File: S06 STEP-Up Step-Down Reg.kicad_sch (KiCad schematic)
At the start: 57 parts, among them Q16 IAUCN04S7L019, Q17 IAUCN04S7L028, Q18 CSD17304Q3, Q19 IAUCN04S7L019, U5 LM51772RHAR

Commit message: Gate resistors placed, snubbers at the low-side FETs in EVM order, H1/H2/LOGO01 symbols
- R111-R114 (3R 0603) placed and routed next to the Q16-Q19 gates, each fed
  from In6 through a via in its driver-side pad.
- Snubbers reordered to match TI's LM51772EVM-HP (switch node -> C -> R -> GND)
  and moved to the low-side FETs: C39 on Q19's drain edge with R45 to GND,
  C35 on Q17's drain leads with R41 to GND, two In1 vias at each R GND pad.
  The top-copper SW1/SW2 pour lobes for the old positions are removed.
- H1, H2 (Mechanical:MountingHole_Pad, pin 1 to GND) and LOGO01 (pinless
  EVOSONIC_LOGO symbol) added to the root sheet and linked to their existing
  footprints, so Update PCB from Schematic no longer deletes them. The
  mounting-hole footprint is saved as MountingHole_3.2mm_Pad_7.4mm.
- ERC 0; DRC 0 unconnected, 0 parity, no courtyard overlaps.

Co-Authored-By: Claude Opus 5.5 <noreply@anthropic.com>
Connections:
- net GND: now also R41.1, R45.1; no longer C35.1, C39.1
- net SW1: now also C35.2; no longer R41.2
- net SW2: now also C39.2; no longer R45.2
- new net: C39.1, R45.2
- new net: C35.1, R41.2
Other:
- moved on the sheet: C35, C39, R41, R45
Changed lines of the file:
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@@
 	(symbol
 		(lib_id "Device:C")
-		(at 227.33 88.9 180)
+		(at 227.33 78.74 180)
 		(unit 1)
 		(body_style 1)
@@
 		(dnp no)
 		(property "Reference" "C39"
-			(at 228.6 88.646 0)
+			(at 228.6 78.486 0)
 			(show_name no)
 			(do_not_autoplace no)
@@
 		)
 		(property "Value" "1nF"
-			(at 228.6 91.186 0)
+			(at 228.6 81.026 0)
 			(show_name no)
 			(do_not_autoplace no)
@@
 		)
 		(property "Footprint" "Capacitor_SMD:C_0805_2012Metric"
-			(at 227.33 88.9 90)
+			(at 227.33 78.74 90)
 			(hide yes)
 			(show_name no)
@@
 		)
 		(property "Datasheet" ""
-			(at 227.33 88.9 90)
+			(at 227.33 78.74 90)
 			(hide yes)
 			(show_name no)
@@
 		)
 		(property "Description" "Capacitor 1nF 50V X7R 0805"
-			(at 227.33 88.9 90)
+			(at 227.33 78.74 90)
 			(hide yes)
 			(show_name no)
@@
 		)
 		(property "NOTE" ""
-			(at 226.822 86.36 0)
+			(at 226.822 76.2 0)
 			(hide yes)
 			(show_name no)
@@
 		)
 		(property "PL_SORT_GROUP" ""
-			(at 226.822 86.36 0)
+			(at 226.822 76.2 0)
 			(hide yes)
 			(show_name no)
@@
 		)
 		(property "MANUFACTURER" ""
-			(at 223.012 85.09 0)
+			(at 223.012 74.93 0)
 			(hide yes)
 			(show_name no)
@@
 		)
 		(property "MANUFACTURER_PN" ""
-			(at 223.012 85.09 0)
+			(at 223.012 74.93 0)
 			(hide yes)
 			(show_name no)
@@
 		)
 		(property "ALTIUM_VALUE" "1nF"
-			(at 224.79 91.44 0)
+			(at 224.79 81.28 0)
 			(hide yes)
 			(show_name no)
@@
 		)
 		(property "ALTIUM_FOOTPRINT" "0805"
-			(at 228.6 93.218 0)
+			(at 228.6 83.058 0)
 			(show_name no)
 			(do_not_autoplace no)
@@
 		)
 		(property "MATERIAL" "X7R"
-			(at 228.6 95.25 0)
+			(at 228.6 85.09 0)
 			(show_name no)
 			(do_not_autoplace no)
@@
 		)
 		(property "VOLTAGE" "50V"
-			(at 228.6 97.79 0)
+			(at 228.6 87.63 0)
 			(show_name no)
 			(do_not_autoplace no)
@@
 	(symbol
 		(lib_id "Device:R")
-		(at 182.88 78.74 180)
+		(at 182.88 88.9 180)
 		(unit 1)
 		(body_style 1)
@@
 		(dnp no)
 		(property "Reference" "R41"
-			(at 183.896 78.74 0)
+			(at 183.896 88.9 0)
 			(show_name no)
 			(do_not_autoplace no)
@@
 		)
 		(property "Value" "2.2R"
-			(at 183.896 81.28 0)
+			(at 183.896 91.44 0)
 			(show_name no)
 			(do_not_autoplace no)
@@
 		)
 		(property "Footprint" "Resistor_SMD:R_1210_3225Metric"
-			(at 182.88 78.74 90)
+			(at 182.88 88.9 90)
 			(hide yes)
 			(show_name no)
@@
 		)
 		(property "Datasheet" ""
-			(at 182.88 78.74 90)
+			(at 182.88 88.9 90)
 			(hide yes)
 			(show_name no)
@@
 		)
 		(property "Description" "Resistor 2.2R 1% 1/2W 1210"
-			(at 182.88 78.74 90)
+			(at 182.88 88.9 90)
 			(hide yes)
 			(show_name no)
@@
 		)
 		(property "NOTE" ""
-			(at 181.864 74.422 0)
+			(at 181.864 84.582 0)
 			(hide yes)
 			(show_name no)
@@
 		)
 		(property "PL_SORT_GROUP" ""
-			(at 181.864 74.422 0)
+			(at 181.864 84.582 0)
 			(hide yes)
 			(show_name no)
@@
 		)
 		(property "MANUFACTURER" ""
-			(at 181.864 74.422 0)
+			(at 181.864 84.582 0)
 			(hide yes)
 			(show_name no)
@@
 		)
 		(property "MANUFACTURER_PN" ""
-			(at 181.864 74.422 0)
+			(at 181.864 84.582 0)
 			(hide yes)
 			(show_name no)
@@
 		)
 		(property "ALTIUM_VALUE" "2.2R"
-			(at 181.864 74.422 0)
+			(at 181.864 84.582 0)
 			(hide yes)
 			(show_name no)
@@
 		)
 		(property "ALTIUM_FOOTPRINT" "1210"
-			(at 183.896 83.312 0)
+			(at 183.896 93.472 0)
 			(show_name no)
 			(do_not_autoplace no)
@@
 	(symbol
 		(lib_id "Device:C")
-		(at 182.88 88.9 180)
+		(at 182.88 78.74 180)
 		(unit 1)
 		(body_style 1)
@@
 		(dnp no)
 		(property "Reference" "C35"
-			(at 184.15 88.646 0)
+			(at 184.15 78.486 0)
 			(show_name no)
 			(do_not_autoplace no)
@@
 		)
 		(property "Value" "470pF"
-			(at 184.15 91.186 0)
+			(at 184.15 81.026 0)
 			(show_name no)
 			(do_not_autoplace no)
@@
 		)
 		(property "Footprint" "Capacitor_SMD:C_0805_2012Metric"
-			(at 182.88 88.9 90)
+			(at 182.88 78.74 90)
 			(hide yes)
 			(show_name no)
@@
 		)
 		(property "Datasheet" ""
-			(at 182.88 88.9 90)
+			(at 182.88 78.74 90)
 			(hide yes)
 			(show_name no)
@@
 		)
 		(property "Description" "Capacitor 470pF 50V X7R 0805"
-			(at 182.88 88.9 90)
+			(at 182.88 78.74 90)
 			(hide yes)
 			(show_name no)
@@
 		)
 		(property "NOTE" ""
-			(at 182.372 86.36 0)
+			(at 182.372 76.2 0)
 			(hide yes)
 			(show_name no)
@@
 		)
 		(property "PL_SORT_GROUP" ""
-			(at 182.372 86.36 0)
+			(at 182.372 76.2 0)
 			(hide yes)
 			(show_name no)
@@
 		)
 		(property "MANUFACTURER" ""
-			(at 178.562 85.09 0)
+			(at 178.562 74.93 0)
 			(hide yes)
 			(show_name no)
@@
 		)
 		(property "MANUFACTURER_PN" ""
-			(at 178.562 85.09 0)
+			(at 178.562 74.93 0)
 			(hide yes)
 			(show_name no)
@@
 		)
 		(property "ALTIUM_VALUE" "470pF"
-			(at 180.34 91.44 0)
+			(at 180.34 81.28 0)
 			(hide yes)
 			(show_name no)
@@
 		)
 		(property "ALTIUM_FOOTPRINT" "0805"
-			(at 184.15 93.218 0)
+			(at 184.15 83.058 0)
 			(show_name no)
 			(do_not_autoplace no)
@@
 		)
 		(property "MATERIAL" "X7R"
-			(at 184.15 95.25 0)
+			(at 184.15 85.09 0)
 			(show_name no)
 			(do_not_autoplace no)
@@
 		)
 		(property "VOLTAGE" "50V"
-			(at 184.15 97.79 0)
+			(at 184.15 87.63 0)
 			(show_name no)
 			(do_not_autoplace no)
@@
 	(symbol
 		(lib_id "Device:R")
-		(at 227.33 78.74 180)
+		(at 227.33 88.9 180)
 		(unit 1)
 		(body_style 1)
@@
 		(dnp no)
 		(property "Reference" "R45"
-			(at 228.346 78.74 0)
+			(at 228.346 88.9 0)
 			(show_name no)
 			(do_not_autoplace no)
@@
 		)
 		(property "Value" "2.2R"
-			(at 228.346 81.28 0)
+			(at 228.346 91.44 0)
 			(show_name no)
 			(do_not_autoplace no)
@@
 		)
 		(property "Footprint" "Resistor_SMD:R_1210_3225Metric"
-			(at 227.33 78.74 90)
+			(at 227.33 88.9 90)
 			(hide yes)
 			(show_name no)
@@
 		)
 		(property "Datasheet" ""
-			(at 227.33 78.74 90)
+			(at 227.33 88.9 90)
 			(hide yes)
 			(show_name no)
@@
 		)
 		(property "Description" "Resistor 2.2R 1% 1/2W 1210"
-			(at 227.33 78.74 90)
+			(at 227.33 88.9 90)
 			(hide yes)
 			(show_name no)
@@
 		)
 		(property "NOTE" ""
-			(at 226.314 74.422 0)
+			(at 226.314 84.582 0)
 			(hide yes)
 			(show_name no)
@@
 		)
 		(property "PL_SORT_GROUP" ""
-			(at 226.314 74.422 0)
+			(at 226.314 84.582 0)
 			(hide yes)
 			(show_name no)
@@
 		)
 		(property "MANUFACTURER" ""
-			(at 226.314 74.422 0)
+			(at 226.314 84.582 0)
 			(hide yes)
 			(show_name no)
@@
 		)
 		(property "MANUFACTURER_PN" ""
-			(at 226.314 74.422 0)
+			(at 226.314 84.582 0)
 			(hide yes)
 			(show_name no)
@@
 		)
 		(property "ALTIUM_VALUE" "2.2R"
-			(at 226.314 74.422 0)
+			(at 226.314 84.582 0)
 			(hide yes)
 			(show_name no)
@@
 		)
 		(property "ALTIUM_FOOTPRINT" "1210"
-			(at 228.346 83.312 0)
+			(at 228.346 93.472 0)
 			(show_name no)
 			(do_not_autoplace no)

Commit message: C60: 100 nF 0603 output HF cap at Q18's drain
Closes the boost hot loop at the FETs, as C7 on TI's LM51772EVM-HP.
Output pad has a via to the inner output planes; GND pad has two vias
to In1.

Co-Authored-By: Claude Opus 5.5 <noreply@anthropic.com>
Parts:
- added C60: 100nF, Capacitor_SMD:C_0603_1608Metric, symbol Device:C
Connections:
- net GND: now also C60.1
- net at C40.1, C41.1, C42.1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: now also C60.2
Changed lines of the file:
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@@
 		)
+	)
+	(symbol
+		(lib_id "Device:C")
+		(at 270.510 76.200 180)
+		(unit 1)
+		(body_style 1)
+		(exclude_from_sim no)
+		(in_bom yes)
+		(on_board yes)
+		(in_pos_files yes)
+		(dnp no)
+		(property "Reference" "C60"
+			(at 271.780 75.946 0)
+			(show_name no)
+			(do_not_autoplace no)
+			(effects
+				(font
+					(size 1.27 1.27)
+				)
+				(justify right bottom)
+			)
+		)
+		(property "Value" "100nF"
+			(at 271.780 78.486 0)
+			(show_name no)
+			(do_not_autoplace no)
+			(effects
+				(font
+					(size 1.27 1.27)
+				)
+				(justify right bottom)
+			)
+		)
+		(property "Footprint" "Capacitor_SMD:C_0603_1608Metric"
+			(at 270.510 76.200 90)
+			(hide yes)
+			(show_name no)
+			(do_not_autoplace no)
+			(effects
+				(font
+					(size 1.27 1.27)
+				)
+			)
+		)
+		(property "Datasheet" ""
+			(at 270.510 76.200 90)
+			(hide yes)
+			(show_name no)
+			(do_not_autoplace no)
+			(effects
+				(font
+					(size 1.27 1.27)
+				)
+			)
+		)
+		(property "Description" "Capacitor 100nF 50V X7R 0603"
+			(at 270.510 76.200 90)
+			(hide yes)
+			(show_name no)
+			(do_not_autoplace no)
+			(effects
+				(font
+					(size 1.27 1.27)
+				)
+			)
+		)
+		(property "NOTE" ""
+			(at 269.240 71.882 0)
+			(hide yes)
+			(show_name no)
+			(do_not_autoplace no)
+			(effects
+				(font
+					(size 1.27 1.27)
+				)
+				(justify right bottom)
+			)
+		)
+		(property "PL_SORT_GROUP" ""
+			(at 269.240 71.882 0)
+			(hide yes)
+			(show_name no)
+			(do_not_autoplace no)
+			(effects
+				(font
+					(size 1.27 1.27)
+				)
+				(justify right bottom)
+			)
+		)
+		(property "MANUFACTURER" ""
+			(at 269.240 71.882 0)
+			(hide yes)
+			(show_name no)
+			(do_not_autoplace no)
+			(effects
+				(font
+					(size 1.27 1.27)
+				)
+				(justify right bottom)
+			)
+		)
+		(property "MANUFACTURER_PN" ""
+			(at 269.240 71.882 0)
+			(hide yes)
+			(show_name no)
+			(do_not_autoplace no)
+			(effects
+				(font
+					(size 1.27 1.27)
+				)
+				(justify right bottom)
+			)
+		)
+		(property "ALTIUM_VALUE" "100nF"
+			(at 269.240 71.882 0)
+			(hide yes)
+			(show_name no)
+			(do_not_autoplace no)
+			(effects
+				(font
+					(size 1.27 1.27)
+				)
+				(justify right bottom)
+			)
+		)
+		(property "ALTIUM_FOOTPRINT" "0603"
+			(at 271.780 80.518 0)
+			(show_name no)
+			(do_not_autoplace no)
+			(effects
+				(font
+					(size 1.27 1.27)
+				)
+				(justify right bottom)
+			)
+		)
+		(property "MATERIAL" "X7R"
+			(at 271.780 82.550 0)
+			(show_name no)
+			(do_not_autoplace no)
+			(effects
+				(font
+					(size 1.27 1.27)
+				)
+				(justify right bottom)
+			)
+		)
+		(property "VOLTAGE" "50V"
+			(at 271.780 85.090 0)
+			(show_name no)
+			(do_not_autoplace no)
+			(effects
+				(font
+					(size 1.27 1.27)
+				)
+				(justify right bottom)
+			)
+		)
+		(pin "2"
+		)
+		(pin "1"
+		)
+		(instances
+			(project "EVO2513"
+				(path "/44203427-0a3b-455b-9bb9-c1b577d179b3/7e883a06-f690-476b-966b-7e93c32ca0bb"
+					(reference "C60")
+					(unit 1)
+				)
+			)
+		)
+	)
+	(wire
+		(pts
+			(xy 270.51 59.69) (xy 270.51 72.39)
+		)
+		(stroke
+			(width 0)
+			(type default)
+		)
+	)
+	(wire
+		(pts
+			(xy 270.51 80.01) (xy 270.51 92.71)
+		)
+		(stroke
+			(width 0)
+			(type default)
+		)
+	)
+	(junction
+		(at 270.51 59.69)
+		(diameter 0)
+		(color 0 0 0 0)
+	)
+	(junction
+		(at 270.51 92.71)
+		(diameter 0)
+		(color 0 0 0 0)
 	)
 )

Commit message: Add BIAS decoupling, sense +12V after R48, move FB divider to U5
- R46/R47 (FB divider) moved next to U5 pin 14, with related routing.
- C61 100 nF 0402 (CC0402KPX7R9BB104) from U5 BIAS (pin 40) to GND,
  between R88 and R89, GND via in pad; as Cbias in TI's WEBENCH design.
- R46 top now on +12V, Kelvin-routed on B.Cu from R48's load-side pad,
  so +12V is regulated after the 5 mOhm shunt (per datasheet Figure 9-1
  and 9.9.1.3). VOUT (pin 18) stays on the power stage.
- REGTEMP on In6 rerouted clear of the GND via at (138.68, 113.70).
- QC box and nearby parts moved.
- README: C61 and R46 rows in the U5 changes table.

DRC: 23 (silk/text only), 0 unconnected, 0 parity; ERC 0.

Co-Authored-By: Claude Opus 5.5 <noreply@anthropic.com>
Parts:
- added C61: 100nF, Capacitor_SMD:C_0402_1005Metric, symbol Device:C
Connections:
- net +12V: now also R46.2
- net BIAS: now also C61.1
- net GND: now also C61.2
- net at C40.1, C41.1, C42.1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: no longer R46.2

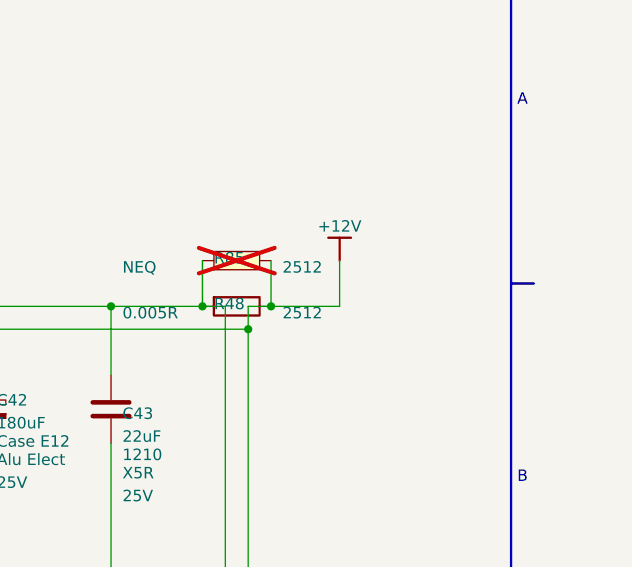
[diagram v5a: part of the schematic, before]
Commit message: Raise divider impedances, dim the PG LEDs, use standard diode lands
TI asks for a pull-up of at least 350 kOhm on EN/UVLO above 5 V.
R108 100K -> 619K and R49 12K -> 75K, both values already on the
BOM: turn-on 11.10 V (10.63-11.91 V worst case), off 10.09 V. 1M/120K
was rejected because leakage across 1M puts worst-case turn-on at
12.24 V, above the rail.

Q24 gate bias R109 100K -> 1.07M and R110 27K -> 390K: +12V draw
94 -> 8.2 uA, gate 3.2 V at 12 V and under 4 V worst case at the
14.7 V OVLO limit. The R115 bypass pull-down is now 62.9K.

PGTH dividers R59/R61/R76 100K -> 390K and R60/R62/R77 13K -> 51K:
PG at 10.38 V (11.17 V worst case), 23.5 uA at threshold to meet TI's
20x PGTH leakage rule. 390K is the only new BOM value.

PG LED resistors R67/R68/R81 2.2K -> 4.7K, about 0.9 mA less on
battery with all rails up.

D1, D4, D6-D10 and LED1-LED4 move from imported Altium lands to KiCad
standard footprints (D_SMB, D_SMA, SOT-23, Diodes_UDFN-10, LED_0603),
in place with the same nets; the LEDs turn 180 deg for pad 1. Drops
the 8 thin LED A/C silk warnings. Five unused imported footprints
removed. Nearby parts and tracks adjusted for the new lands.

Keep the GND planes free of power copper, as on the original: remove
the SW1/L2 and SW2 strip zones and the small +12V (via block by R115)
and U5 ISNSP (under Q18's drain) zones from In1/In3/In5/In6. They
carried no current; GND gains about 0.8 mm2 on In1, 3.5 mm2 on In3
and In5 and 3.7 mm2 on In6 under the power stage.

Remove the 347 via-block octagons the Altium import left as copper
graphic polygons (gr_poly) on B.Cu and In1-In6, one 1.2 x 1.8 mm
octagon per six-via block per layer. As drawings they bypassed zone
rules, and on the GND layers they were net islands in the pour,
including the charger switch node. None carried current: same-net
pours connect the vias solid, and DRC finds 0 unconnected. GND gains
about 26 mm2 on In1, 21 mm2 on In3 and In5, 18 mm2 on In6 and 27 mm2
on B.Cu.

Rename TPS22811 pin 2 to nEN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
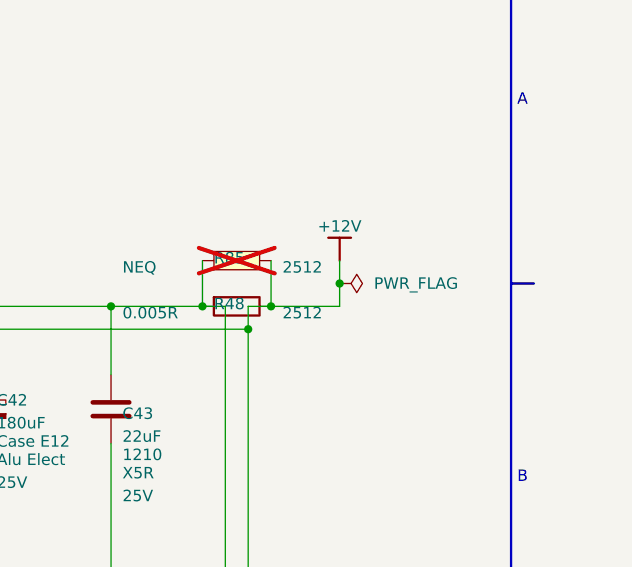
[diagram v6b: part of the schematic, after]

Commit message: Fill manufacturer part numbers from the 0.5.0 build orders
Set MANUFACTURER and MANUFACTURER_PN on every fitted part, in the
schematic and on the board. Unchanged parts take the exact part numbers
ordered for the 0.5.0 backup build (DigiKey list and Mouser basket);
changed parts reuse an ordered part where value, package and rating
match; the rest keep the schematic's part or take a Yageo RC/CC part.

Co-Authored-By: Claude Opus 5.5 <noreply@anthropic.com>
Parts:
- C27, C32: MANUFACTURER Murata -> Murata Electronics
- C28, C40, C41, C42: MANUFACTURER Panasonic -> Panasonic Industry
- C29: MANUFACTURER (none) -> YAGEO; MANUFACTURER_PN (none) -> CC0402KRX7R8BB683
- C31: MANUFACTURER (none) -> YAGEO; MANUFACTURER_PN (none) -> CC0402JRNPO9BN181
- C33: MANUFACTURER (none) -> YAGEO; MANUFACTURER_PN (none) -> CC0402KRX7R9BB153
- C34, C37, C38, C61: MANUFACTURER Yageo -> YAGEO
- C35: MANUFACTURER (none) -> YAGEO; MANUFACTURER_PN (none) -> CC0805KRX7R9BB471
- C36: MANUFACTURER (none) -> YAGEO; MANUFACTURER_PN (none) -> CC0402JRNPO9BN111
- C39: MANUFACTURER (none) -> YAGEO; MANUFACTURER_PN (none) -> CC0805KRX7R9BB102
- C43: MANUFACTURER (none) -> Samsung Electro-Mechanics; MANUFACTURER_PN (none) -> CL32A226KAJNNWE
- C60: MANUFACTURER (none) -> YAGEO; MANUFACTURER_PN (none) -> CC0603KRX7R9BB104
- Q16, Q17, Q19: MANUFACTURER Infineon -> Infineon Technologies
- R102, R106, R107: MANUFACTURER ? -> YAGEO; MANUFACTURER_PN ? -> RC0402FR-0710KL
- R104, R105, R38, R86, R87, R88, R89: MANUFACTURER ? -> YAGEO; MANUFACTURER_PN ? -> RC0402JR-070RL
- R111, R112, R113, R114: MANUFACTURER Vishay -> Vishay Dale
- R29: MANUFACTURER (none) -> YAGEO; MANUFACTURER_PN (none) -> RC0402FR-071K87L
- R30: MANUFACTURER ? -> YAGEO; MANUFACTURER_PN ? -> RC0402FR-075K1L
- R31: MANUFACTURER ? -> Panasonic Industry; MANUFACTURER_PN ? -> ERJ-2RKF4022X
- R32: MANUFACTURER (none) -> YAGEO; MANUFACTURER_PN (none) -> RC0402FR-074K22L
- R33: MANUFACTURER ? -> YAGEO; MANUFACTURER_PN ? -> RC0402FR-0775KL
- R34: MANUFACTURER (none) -> YAGEO; MANUFACTURER_PN (none) -> RC0402FR-0713KL
- R35: MANUFACTURER (none) -> YAGEO; MANUFACTURER_PN (none) -> RC0402FR-072K7L
- R36: MANUFACTURER (none) -> YAGEO; MANUFACTURER_PN (none) -> RC0402FR-0761K9L
- R37, R47: MANUFACTURER (none) -> YAGEO; MANUFACTURER_PN (none) -> RC0402FR-075K62L
- R39: MANUFACTURER ? -> YAGEO; MANUFACTURER_PN ? -> RC0402FR-0727KL
- R40: MANUFACTURER ? -> YAGEO; MANUFACTURER_PN ? -> RC0402FR-07100KL
- R41, R45: MANUFACTURER (none) -> YAGEO; MANUFACTURER_PN (none) -> RC1210FR-072R2L
- R42: MANUFACTURER (none) -> Littelfuse Inc.
- R43, R44: MANUFACTURER ? -> YAGEO; MANUFACTURER_PN ? -> RC0402FR-0710RL
- R46: MANUFACTURER (none) -> YAGEO; MANUFACTURER_PN (none) -> RC0402FR-0762KL
- R48: MANUFACTURER (none) -> Bourns Inc.
